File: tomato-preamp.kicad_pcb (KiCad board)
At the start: 2 copper layers, 77 x 69.8 mm, 23 parts, among them J1 IN, J2 OUT, J3.1 +ANODE, J3.2 -ANODE, J4.1 +HEATER, J4.2 -HEATER, U1 6N2P

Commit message: Rewire
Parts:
- added C7: 22u 400V, Capacitor_THT:CP_Radial_D13.0mm_P7.50mm, F.Cu at (131.4, 89.4)
- added C8: 22u 400V, Capacitor_THT:CP_Radial_D13.0mm_P7.50mm, F.Cu at (114.7, 89.3)
- added R10: 1K 2W, Resistor_THT:R_Axial_DIN0516_L15.5mm_D5.0mm_P20.32mm_Horizontal, F.Cu at (107.8, 75.4)
- added R11: 1K, Resistor_THT:R_Axial_DIN0207_L6.3mm_D2.5mm_P10.16mm_Horizontal, F.Cu at (172.2, 84.3)
- added R12: 1K, Resistor_THT:R_Axial_DIN0207_L6.3mm_D2.5mm_P10.16mm_Horizontal, F.Cu at (172.2, 108.7)
- added R9: 1K 2W, Resistor_THT:R_Axial_DIN0516_L15.5mm_D5.0mm_P20.32mm_Horizontal, F.Cu at (129.8, 96.1)
- R4, R7: value 32k -> 32k 2W
- moved R5 60.3 mm to (132.9, 128.9), turned to 90 degrees
- moved R6 46.2 mm to (159.3, 127.7)
- moved C3 34.0 mm to (127.5, 108.4)
- moved R7 20.8 mm to (132.6, 75.6)
- moved R1 19.1 mm to (149.1, 123.2), turned to 90 degrees
- moved C4 18.4 mm to (168.3, 108.6), turned to 90 degrees
- moved J2 15.3 mm to (118.4, 69.2)
- moved R2 15.2 mm to (144.4, 123.2), turned to 90 degrees
- moved R3 14.9 mm to (162.8, 113.6), turned to 180 degrees
- moved C6 12.1 mm to (159.0, 84.4), turned to 90 degrees
- moved C2 10.6 mm to (139.3, 104.2), turned to -90 degrees
- moved RV1 8.08 mm to (172.2, 116.0)
- moved U1 7.98 mm to (162.7, 92.8)
- moved J4.1 5.70 mm to (140.2, 97.3)
- moved J4.2 5.70 mm to (140.3, 92.9)
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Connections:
- J3.1 pad 1: /High voltage -> Net-(J3.1-Pin_1)
- R4 pad 2: /High voltage -> Net-(C8-Pad1)
- R7 pad 1: /High voltage -> Net-(C7-Pad1)
- RV1 pad 3: GND -> Net-(R12-Pad1)
- RV2 pad 3: GND -> Net-(R11-Pad1)
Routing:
- net Net-(C8-Pad1): track 0.00 -> 33.1 mm
- net Net-(C7-Pad1): track 0.00 -> 28.8 mm
- net /High voltage: track 24.4 -> 0.00 mm
- net Net-(J1-PadT): track 13.0 -> 35.7 mm
- net Net-(R12-Pad1): track 0.00 -> 21.2 mm
- net Net-(U1B-A): track 41.5 -> 21.3 mm
- net Net-(C2-Pad2): track 34.3 -> 14.2 mm
- net GND: track 253.7 -> 237.6 mm
- net Net-(C3-Pad2): track 29.7 -> 19.4 mm
- net Net-(U1B-G): track 34.3 -> 44.4 mm
- net Net-(C6-Pad2): track 27.1 -> 17.9 mm
- net Net-(J2-PadT): track 63.3 -> 55.3 mm
- net Net-(C4-Pad1): track 34.6 -> 26.7 mm
- net Net-(R11-Pad1): track 0.00 -> 6.39 mm
- net Net-(J3.1-Pin_1): track 0.00 -> 4.22 mm
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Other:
- board size 77 x 69.8 mm -> 77 x 82 mm

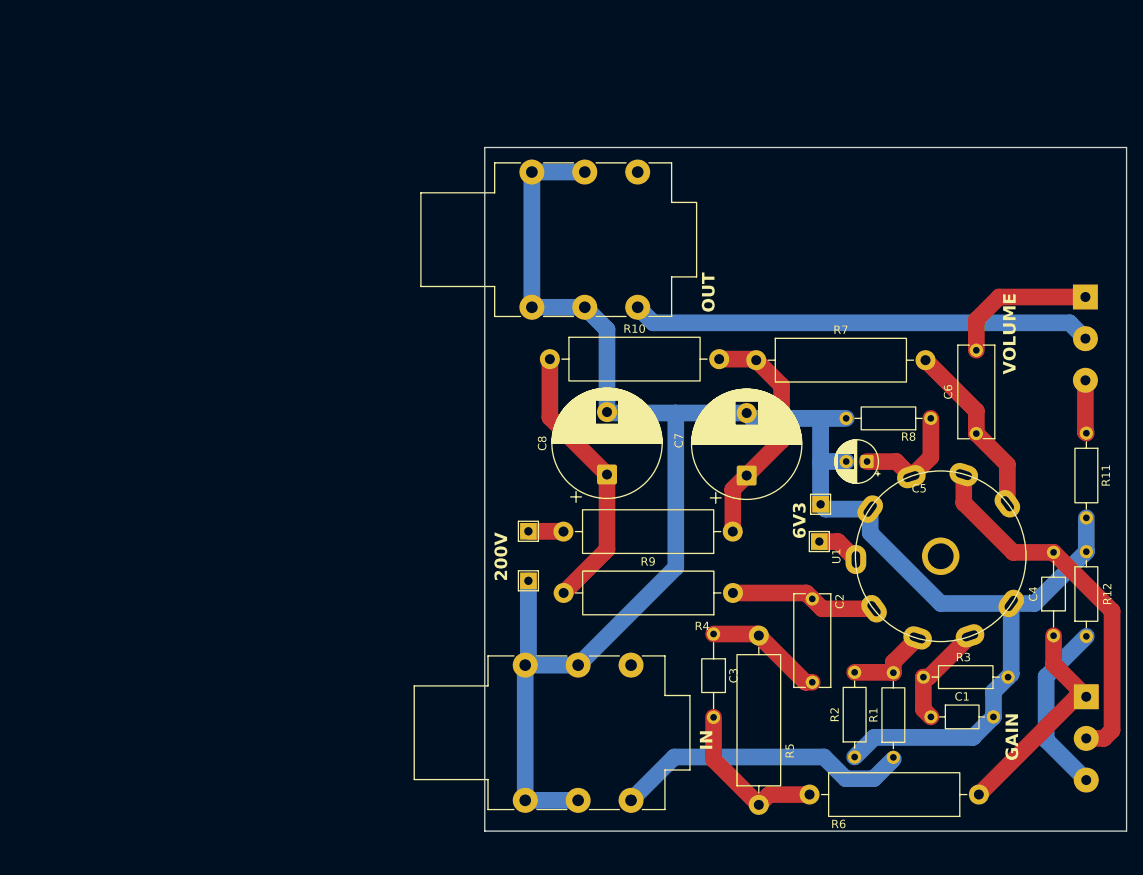
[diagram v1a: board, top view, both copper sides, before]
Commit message: Update footprints
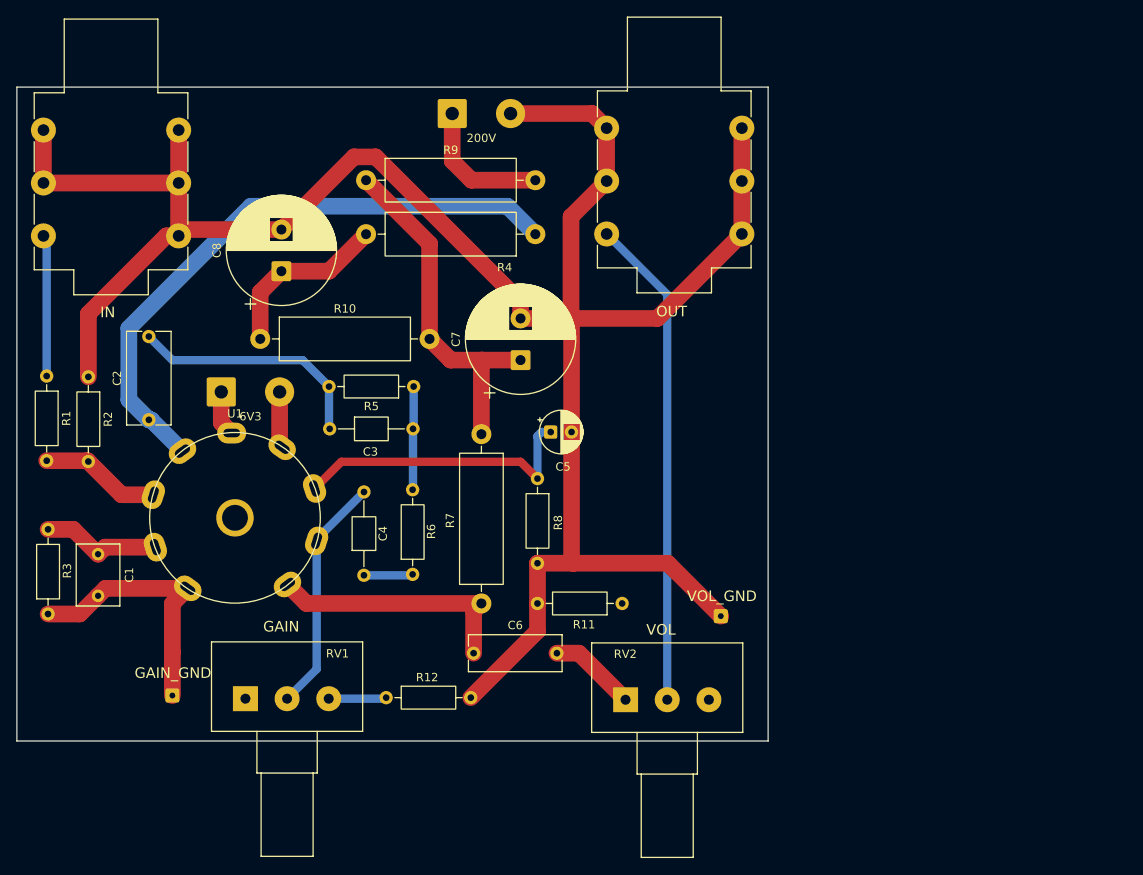
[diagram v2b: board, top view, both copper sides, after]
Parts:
- removed J3.1: +ANODE, TestPoint:TestPoint_THTPad_2.0x2.0mm_Drill1.0mm
- removed J3.2: -ANODE, TestPoint:TestPoint_THTPad_2.0x2.0mm_Drill1.0mm
- removed J4.1: +HEATER, TestPoint:TestPoint_THTPad_2.0x2.0mm_Drill1.0mm
- removed J4.2: -HEATER, TestPoint:TestPoint_THTPad_2.0x2.0mm_Drill1.0mm
- added J3: 200V, Connector_Wire:SolderWire-0.75sqmm_1x02_P7mm_D1.25mm_OD3.5mm, F.Cu at (96.1, 46.0)
- added J4: 6V3, Connector_Wire:SolderWire-0.75sqmm_1x02_P7mm_D1.25mm_OD3.5mm, F.Cu at (68.4, 79.4)
- added J5: GAIN_GND, Connector_Wire:SolderWire-0.127sqmm_1x01_D0.48mm_OD1mm, F.Cu at (62.5, 115.8)
- added J6: VOL_GND, Connector_Wire:SolderWire-0.127sqmm_1x01_D0.48mm_OD1mm, F.Cu at (128.3, 106.3)
- C1: footprint Capacitor_THT:C_Axial_L3.8mm_D2.6mm_P7.50mm_Horizontal -> Capacitor_THT:C_Rect_L7.2mm_W5.0mm_P5.00mm
- C2: footprint Capacitor_THT:C_Rect_L11.0mm_W4.2mm_P10.00mm_MKT -> Capacitor_THT:C_Rect_L11.0mm_W5.1mm_P10.00mm_MKT
- C7, C8: footprint Capacitor_THT:CP_Radial_D13.0mm_P7.50mm -> Capacitor_THT:CP_Radial_D13.0mm_P5.00mm
- R5, R6: footprint Resistor_THT:R_Axial_DIN0516_L15.5mm_D5.0mm_P20.32mm_Horizontal -> Resistor_THT:R_Axial_DIN0207_L6.3mm_D2.5mm_P10.16mm_Horizontal
- RV1, RV2: moved to F.Cu
- moved R3 115.5 mm to (47.6, 106.0), turned to 90 degrees
- moved R1 111.5 mm to (47.4, 77.5), turned to -90 degrees
- moved R2 102.7 mm to (52.4, 77.6), turned to -90 degrees
- moved C1 101.9 mm to (53.6, 98.8), turned to -90 degrees
- moved RV1 100.9 mm to (71.3, 116.2), turned to 90 degrees
- moved J1 97.8 mm to (47.0, 60.6), turned to 90 degrees
- moved U1 86.9 mm to (76.3, 102.5), turned to 0 degrees
- moved R12 84.4 mm to (88.2, 116.1), turned to 0 degrees
- moved C4 83.1 mm to (85.5, 101.4)
- moved C2 82.5 mm to (59.7, 82.7), turned to 90 degrees
- moved RV2 73.4 mm to (116.9, 116.3), turned to 90 degrees
- moved R6 72.9 mm to (91.3, 101.3), turned to 90 degrees
- moved C6 65.8 mm to (98.7, 110.7), turned to 0 degrees
- moved R5 65.1 mm to (91.5, 78.7), turned to 180 degrees
- moved R9 61.0 mm to (85.8, 54.0), turned to 0 degrees
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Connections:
- J1 pad TN: unconnected-(J1-PadTN) -> GND
- J2 pad TN: unconnected-(J2-PadTN) -> GND
- U1 pad 4: GND -> Net-(J4-Pin_2)
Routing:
- net GND: track 237.6 -> 297.3 mm
- net Net-(U1A-A): track 17.7 -> 73.8 mm
- net Net-(U1B-K): track 14.0 -> 35.8 mm
- net Net-(C4-Pad1): track 26.7 -> 5.89 mm
- net Net-(J1-PadT): track 35.7 -> 17.0 mm
- net Net-(U1B-G): track 44.4 -> 28.6 mm
- net Net-(C2-Pad2): track 14.2 -> 29.2 mm
- net Net-(C7-Pad1): track 28.8 -> 43.1 mm
- net Net-(R12-Pad1): track 21.2 -> 6.94 mm
- net Net-(J3-Pin_1): track 4.22 -> 16.6 mm
- net Net-(C8-Pad1): track 33.1 -> 21.2 mm
- net Net-(U1B-A): track 21.3 -> 30.6 mm
- net Net-(C6-Pad2): track 17.9 -> 10.6 mm
- net Net-(C3-Pad2): track 19.4 -> 12.4 mm
- net Net-(J4-Pin_2): track 0.00 -> 6.77 mm
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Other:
- board size 77 x 82 mm -> 90.2 x 78.5 mm
- board text removed: "200V"
- board text removed: "6V3"
- board text removed: "GAIN"
- board text removed: "IN"
- board text removed: "OUT"
- board text removed: "VOLUME"
